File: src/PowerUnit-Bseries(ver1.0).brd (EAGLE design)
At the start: 112.7 x 77 mm, 46 parts

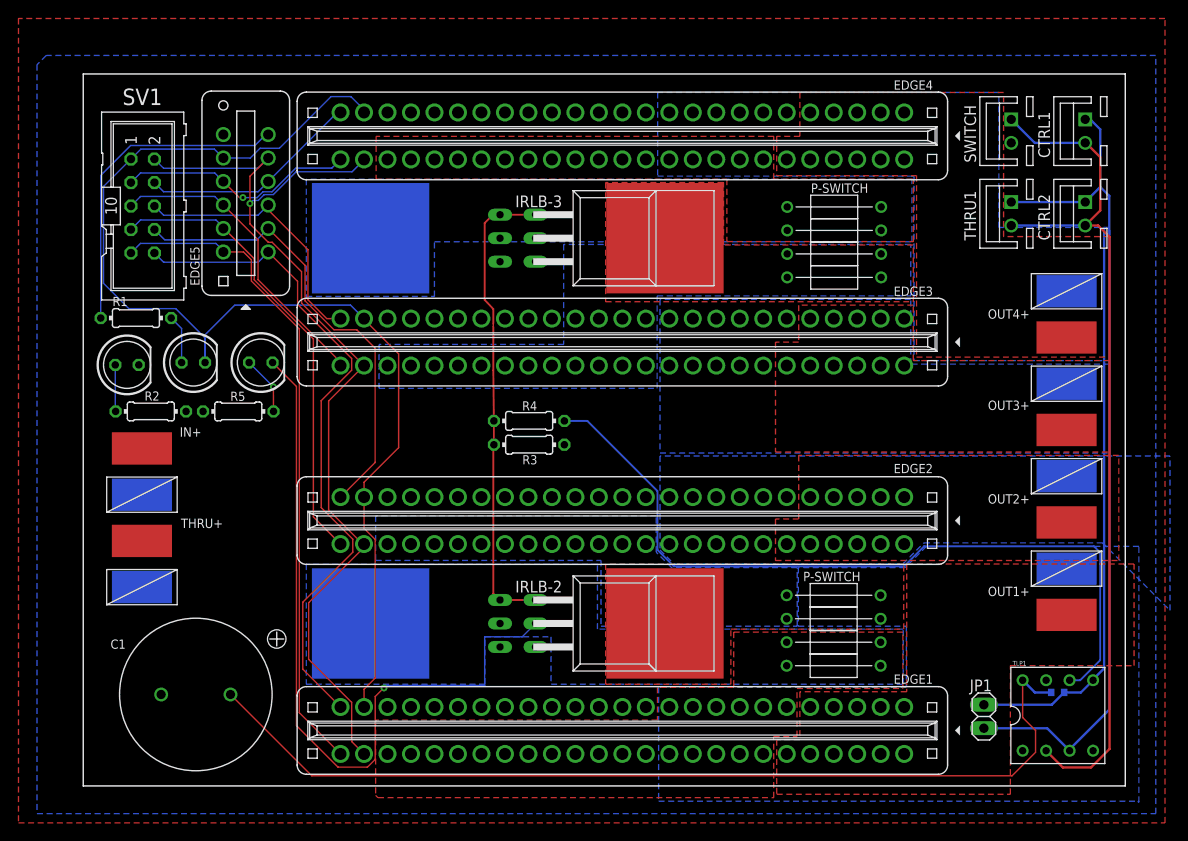
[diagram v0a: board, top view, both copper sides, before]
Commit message: 再設計 Edgeコネクタを40Pにした
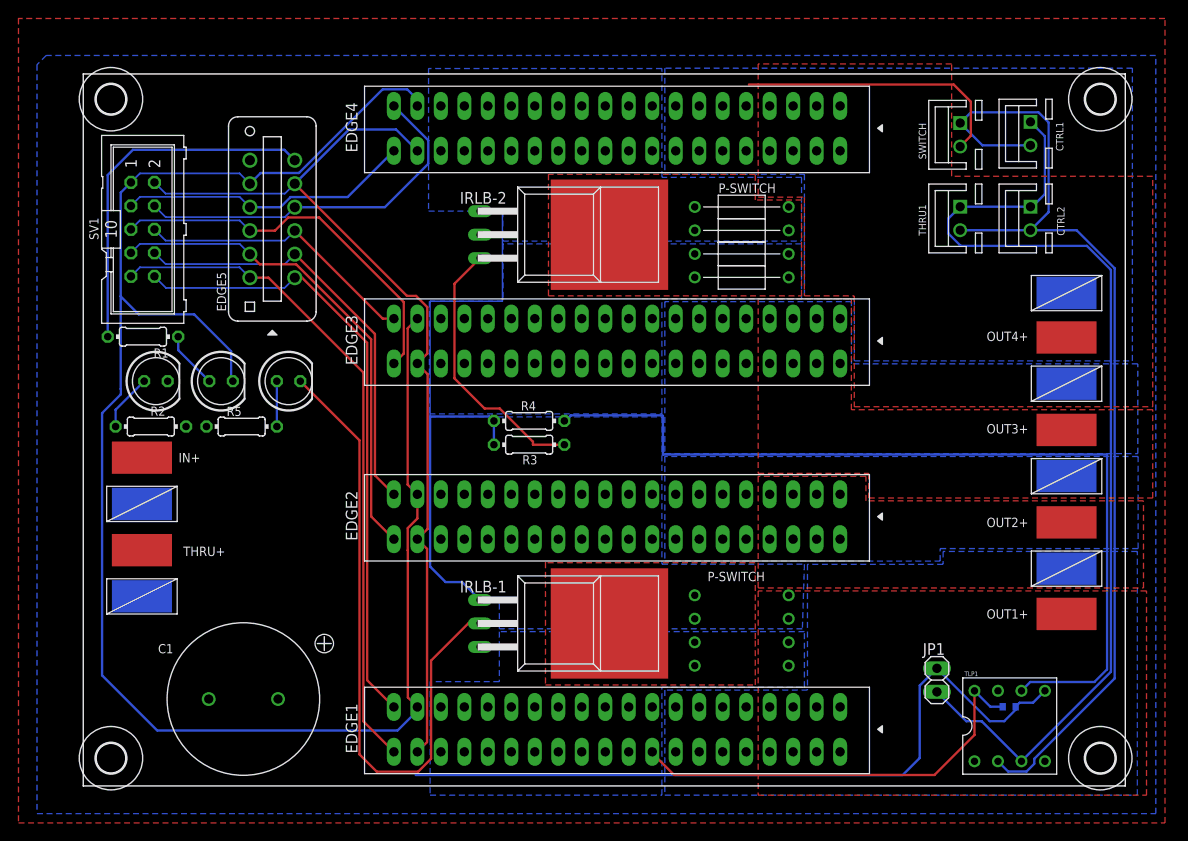
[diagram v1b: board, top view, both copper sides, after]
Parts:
- removed IRLB-3, IRLB-4: IRLB3813_2, OKUDA_libraries:TO-220AB-PUT
- added H1, H2, H3, H4: MOUNT-HOLE3.2, holes:3,2
- EDGE1, EDGE2, EDGE3, EDGE4: value 10046971-019LF-FEMAL -> EDGE20X2; device 10046971-019LF-FEMAL:10046971-019LF -> Edge20x2:EDGE20X2
- moved IRLB-2 42.5 mm to (48.0, 59.6)
- moved P-5 10.0 mm to (73.8, 55.0)
- moved P-6 10.0 mm to (73.8, 57.5)
- moved P-7 10.0 mm to (73.8, 60.1)
- moved P-8 10.0 mm to (73.8, 62.6)
- moved IRLB-1 8.00 mm to (48.0, 17.6), flipped to the top
- moved JP1 6.43 mm to (92.3, 11.4)
- moved CTRL2 5.94 mm to (102.4, 61.4)
- moved CTRL1 5.93 mm to (102.4, 70.5)
- moved THRU1 5.55 mm to (94.8, 61.4)
- moved SWITCH 5.54 mm to (94.8, 70.4)
- moved C2 5.47 mm to (100.1, 8.56)
- moved TLP1 5.33 mm to (100.2, 6.48)
- moved C1 5.17 mm to (17.3, 9.40)
- moved P-1 4.86 mm to (73.8, 13.0), flipped to the bottom
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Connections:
- removed net N$10: EDGE4.P$1, EDGE4.P$2, EDGE4.P$3, EDGE4.P$4, EDGE4.P$45, EDGE4.P$46, EDGE4.P$47, EDGE4.P$48, EDGE4.P$49, EDGE4.P$5, EDGE4.P$50, OUT4+.P$1
- removed net N$12: IRLB-4.P$1, P-7.P$2, P-8.P$2
- removed net N$13: EDGE4.P$10, EDGE4.P$11, EDGE4.P$40, EDGE4.P$41, EDGE4.P$42, EDGE4.P$43, EDGE4.P$44, EDGE4.P$6, EDGE4.P$7, EDGE4.P$8, EDGE4.P$9, OUT4-.P$1
- removed net N$14: EDGE3.P$28, EDGE3.P$29, EDGE3.P$30, EDGE3.P$31, EDGE3.P$32, EDGE3.P$33, EDGE3.P$34, EDGE3.P$35, EDGE3.P$36, EDGE3.P$37, EDGE3.P$38, EDGE3.P$39, P-5.P$1, P-6.P$1
- removed net N$15: IRLB-3.P$1, P-5.P$2, P-6.P$2
- removed net N$25: EDGE1.P$28, EDGE1.P$29, EDGE1.P$30, EDGE1.P$31, EDGE1.P$32, EDGE1.P$33, EDGE1.P$34, EDGE1.P$35, EDGE1.P$36, EDGE1.P$37, EDGE1.P$38, EDGE1.P$39, P-1.P$1, P-2.P$1
- removed net N$26: EDGE2.P$28, EDGE2.P$29, EDGE2.P$30, EDGE2.P$31, EDGE2.P$32, EDGE2.P$33, EDGE2.P$34, EDGE2.P$35, EDGE2.P$36, EDGE2.P$37, EDGE2.P$38, EDGE2.P$39, P-3.P$1, P-4.P$1
- new net N$23: IRLB-1.P$1, P-1.P$2, P-2.P$2, P-3.P$2, P-4.P$2
- new net N$27: IRLB-2.P$1, P-5.P$2, P-6.P$2, P-7.P$2, P-8.P$2
- new net N$28: EDGE1.P$1, EDGE1.P$2, EDGE1.P$3, EDGE1.P$37, EDGE1.P$38, EDGE1.P$39, EDGE1.P$4, EDGE1.P$40, OUT1+.P$1
- new net N$34: EDGE2.P$14, EDGE2.P$15, EDGE2.P$16, EDGE2.P$17, EDGE2.P$18, EDGE2.P$23, EDGE2.P$24, EDGE2.P$25, EDGE2.P$26, EDGE2.P$27, P-3.P$1, P-4.P$1
- new net N$35: EDGE3.P$1, EDGE3.P$2, EDGE3.P$3, EDGE3.P$37, EDGE3.P$38, EDGE3.P$39, EDGE3.P$4, EDGE3.P$40, OUT3+.P$1
- net DIR1: now also EDGE1.P$21; no longer EDGE1.P$26
- net DIR2: now also EDGE2.P$21; no longer EDGE2.P$26
- net DIR3: now also EDGE3.P$21; no longer EDGE3.P$26
- net DIR4: now also EDGE4.P$21; no longer EDGE4.P$26
- net GND: no longer IRLB-3.S, IRLB-4.S
- net GND2: now also EDGE1.P$19, EDGE2.P$19, EDGE3.P$19, EDGE4.P$19; no longer EDGE1.P$24, EDGE2.P$24, EDGE3.P$24, EDGE4.P$24
- net N$1: now also EDGE1.P$33, EDGE1.P$34, EDGE1.P$35, EDGE1.P$36, EDGE1.P$5; no longer EDGE1.P$10, EDGE1.P$11, EDGE1.P$40, EDGE1.P$41, EDGE1.P$42, EDGE1.P$43, EDGE1.P$44, EDGE1.P$9
- net N$11: now also EDGE4.P$14, EDGE4.P$15, EDGE4.P$16, EDGE4.P$17, EDGE4.P$18, EDGE4.P$23, EDGE4.P$24, EDGE4.P$25, EDGE4.P$26, EDGE4.P$27, P-7.P$1, P-8.P$1; no longer IRLB-2.P$1, P-3.P$2, P-4.P$2
- net N$2: now also EDGE2.P$33, EDGE2.P$34, EDGE2.P$35, EDGE2.P$36, EDGE2.P$5; no longer EDGE2.P$10, EDGE2.P$11, EDGE2.P$40, EDGE2.P$41, EDGE2.P$42, EDGE2.P$43, EDGE2.P$44, EDGE2.P$9
- net N$22: no longer IRLB-3.G, IRLB-4.G
- net N$24: now also IRLB-1.D; no longer IRLB-2.D
- net N$4: now also EDGE1.P$14, EDGE1.P$15, EDGE1.P$16, EDGE1.P$17, EDGE1.P$18, EDGE1.P$23, EDGE1.P$24, EDGE1.P$25, EDGE1.P$26, EDGE1.P$27, P-1.P$1, P-2.P$1; no longer EDGE1.P$1, EDGE1.P$2, EDGE1.P$3, EDGE1.P$4, EDGE1.P$45, EDGE1.P$46, EDGE1.P$47, EDGE1.P$48, EDGE1.P$49, EDGE1.P$5, EDGE1.P$50, OUT1+.P$1
- net N$5: now also EDGE2.P$37, EDGE2.P$38, EDGE2.P$39, EDGE2.P$40; no longer EDGE2.P$45, EDGE2.P$46, EDGE2.P$47, EDGE2.P$48, EDGE2.P$49, EDGE2.P$5, EDGE2.P$50
- net N$6: now also EDGE4.P$33, EDGE4.P$34, EDGE4.P$35, EDGE4.P$36, EDGE4.P$5, EDGE4.P$6, EDGE4.P$7, EDGE4.P$8, OUT4-.P$1; no longer EDGE3.P$1, EDGE3.P$2, EDGE3.P$3, EDGE3.P$4, EDGE3.P$45, EDGE3.P$46, EDGE3.P$47, EDGE3.P$48, EDGE3.P$49, EDGE3.P$5, EDGE3.P$50, OUT3+.P$1
- net N$7: now also EDGE3.P$33, EDGE3.P$34, EDGE3.P$35, EDGE3.P$36, EDGE3.P$5, EDGE3.P$6, EDGE3.P$7, EDGE3.P$8, OUT3-.P$1; no longer IRLB-1.P$1, P-1.P$2, P-2.P$2
- net N$8: now also EDGE4.P$1, EDGE4.P$2, EDGE4.P$3, EDGE4.P$4, EDGE4.P$40, OUT4+.P$1; no longer EDGE4.P$28, EDGE4.P$29, EDGE4.P$30, EDGE4.P$31, EDGE4.P$32, EDGE4.P$33, EDGE4.P$34, EDGE4.P$35, EDGE4.P$36, P-7.P$1, P-8.P$1
- net N$9: now also EDGE3.P$14, EDGE3.P$15, EDGE3.P$16, EDGE3.P$17, EDGE3.P$18, EDGE3.P$23, EDGE3.P$24, EDGE3.P$25, EDGE3.P$26, EDGE3.P$27, P-5.P$1, P-6.P$1; no longer EDGE3.P$10, EDGE3.P$11, EDGE3.P$40, EDGE3.P$41, EDGE3.P$42, EDGE3.P$43, EDGE3.P$44, EDGE3.P$6, EDGE3.P$7, EDGE3.P$8, EDGE3.P$9, OUT3-.P$1
- net PWM1: now also EDGE1.P$20; no longer EDGE1.P$25
- net PWM2: now also EDGE2.P$20; no longer EDGE2.P$25
- net PWM3: now also EDGE3.P$20; no longer EDGE3.P$25
- net PWM4: now also EDGE4.P$20; no longer EDGE4.P$25
- net VCC: now also EDGE1.P$10, EDGE1.P$11, EDGE1.P$28, EDGE1.P$29, EDGE1.P$30, EDGE1.P$31, EDGE1.P$32, EDGE1.P$9, EDGE2.P$10, EDGE2.P$11, EDGE2.P$28, EDGE2.P$29, EDGE2.P$30, EDGE2.P$31, EDGE2.P$32, EDGE2.P$9, EDGE3.P$10, EDGE3.P$11, EDGE3.P$28, EDGE3.P$29, EDGE3.P$30, EDGE3.P$31, EDGE3.P$32, EDGE3.P$9, EDGE4.P$10, EDGE4.P$11, EDGE4.P$28, EDGE4.P$29, EDGE4.P$30, EDGE4.P$31, EDGE4.P$32, EDGE4.P$9; no longer EDGE1.P$14, EDGE1.P$15, EDGE1.P$16, EDGE1.P$17, EDGE1.P$18, EDGE1.P$19, EDGE1.P$20, EDGE1.P$21, EDGE1.P$22, EDGE1.P$23, EDGE2.P$14, EDGE2.P$15, EDGE2.P$16, EDGE2.P$17, EDGE2.P$18, EDGE2.P$19, EDGE2.P$20, EDGE2.P$21, EDGE2.P$22, EDGE2.P$23, EDGE3.P$14, EDGE3.P$15, EDGE3.P$16, EDGE3.P$17, EDGE3.P$18, EDGE3.P$19, EDGE3.P$20, EDGE3.P$21, EDGE3.P$22, EDGE3.P$23, EDGE4.P$14, EDGE4.P$15, EDGE4.P$16, EDGE4.P$17, EDGE4.P$18, EDGE4.P$19, EDGE4.P$20, EDGE4.P$21, EDGE4.P$22, EDGE4.P$23
- net VCC2: now also EDGE1.P$22, EDGE2.P$22, EDGE3.P$22, EDGE4.P$22; no longer EDGE1.P$27, EDGE2.P$27, EDGE3.P$27, EDGE4.P$27
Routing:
- net GND2: track 128.7 -> 191.5 mm
- net GND: track 62.2 -> 111.6 mm
- net VCC: track 103.8 -> 76.4 mm
- net N$21: track 92.0 -> 110.2 mm
- net N$19: track 94.3 -> 111.9 mm
- net PWM4: track 24.1 -> 40.3 mm
- net N$22: track 51.2 -> 65.2 mm
- net N$24: track 81.6 -> 69.7 mm, vias 1 -> 0
- net N$20: track 85.2 -> 96.6 mm
- net DIR3: track 33.4 -> 41.8 mm
- net DIR4: track 25.9 -> 31.8 mm, vias 1 -> 0
- net PWM1: track 72.9 -> 67.5 mm
- net LED: track 35.4 -> 39.3 mm
- net PWM2: track 50.1 -> 46.6 mm
- net VCC2: track 106.4 -> 103.0 mm, vias 1 -> 0
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- added copper zone on layer 16, net N$11
- added copper zone on layer 1, net N$23
- added copper zone on layer 1, net N$27
- added copper zone on layer 1, net N$28
- added copper zone on layer 16, net N$34
- added copper zone on layer 1, net N$35
- added copper zone on layer 16, net N$4
- added copper zone on layer 16, net N$6
- removed copper zone on layer 1, net N$10
- removed copper zone on layer 1, net N$11
- removed copper zone on layer 16, net N$12
- removed copper zone on layer 16, net N$13
- removed copper zone on layer 16, net N$14
- removed copper zone on layer 1, net N$15
- removed copper zone on layer 1, net N$25
- removed copper zone on layer 16, net N$26
- removed copper zone on layer 1, net N$4
- removed copper zone on layer 1, net N$6
